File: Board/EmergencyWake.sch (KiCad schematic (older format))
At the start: 138 parts, among them J1 USB_C_Receptacle_USB2.0, J10 Conn_01x04, J2 Micro_SD_Card_Det, J3 Conn_01x03, J4 Conn_01x02, J5 Conn_01x05, J6 Conn_01x04, J7 Conn_01x02, J8 Conn_01x04, J9 Conn_01x04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

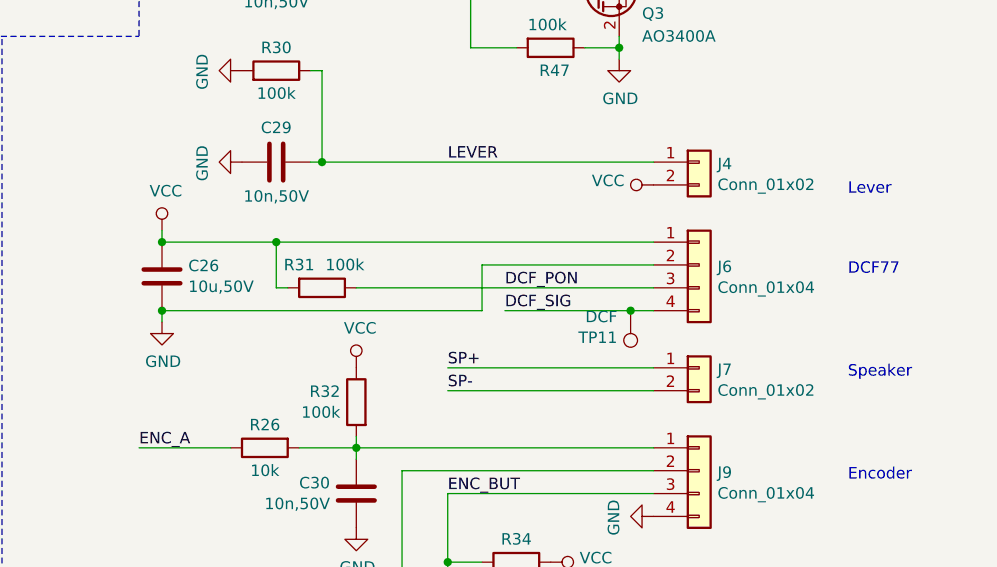
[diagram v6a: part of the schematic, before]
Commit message: [Board] More routing
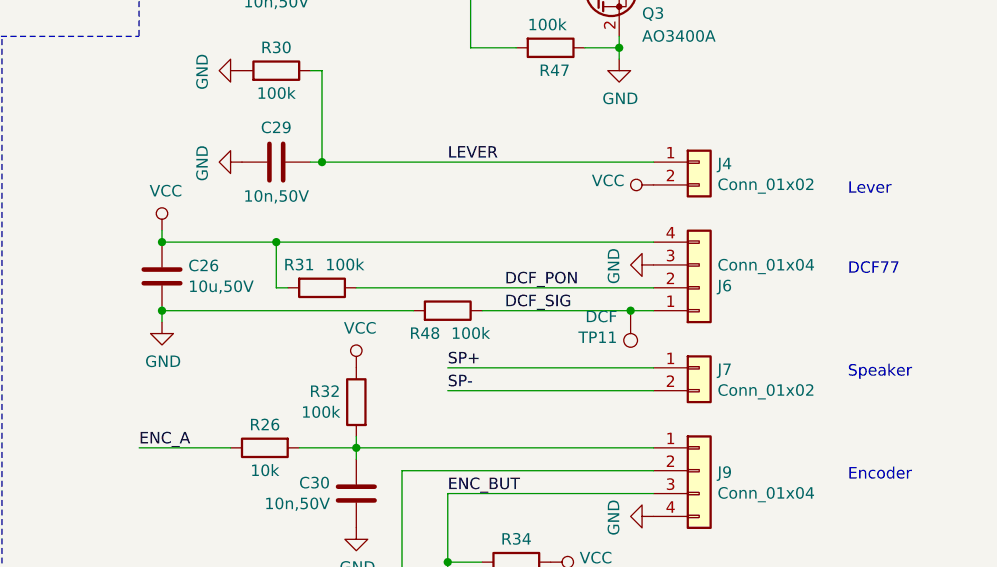
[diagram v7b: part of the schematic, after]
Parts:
- added R48: 100k, Resistor_SMD:R_0402_1005Metric, symbol Device:R
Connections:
- net DCF_PON: now also J6.2 (Pin_2); no longer J6.3 (Pin_3)
- net DCF_SIG: now also J6.1 (Pin_1), R48.1; no longer J6.4 (Pin_4)
- net GND: now also J6.3 (Pin_3), R48.2; no longer J6.2 (Pin_2)
- net VCC: now also J6.4 (Pin_4); no longer J6.1 (Pin_1)
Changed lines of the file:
@@
 L Connector_Generic:Conn_01x04 J6
 U 1 1 5E489DA8
-P 13900 3300
-F 0 "J6" H 13980 3292 50  0000 L CNN
-F 1 "Conn_01x04" H 13980 3201 50  0000 L CNN
-F 2 "Connector_PinHeader_2.54mm:PinHeader_1x04_P2.54mm_Horizontal" H 13900 3300 50  0001 C CNN
-F 3 "~" H 13900 3300 50  0001 C CNN
-	1    13900 3300
-	1    0    0    -1
+P 13900 3400
+F 0 "J6" H 13980 3392 50  0000 L CNN
+F 1 "Conn_01x04" H 13980 3301 50  0000 L CNN
+F 2 "Connector_PinHeader_2.54mm:PinHeader_1x04_P2.54mm_Horizontal" H 13900 3400 50  0001 C CNN
+F 3 "~" H 13900 3400 50  0001 C CNN
+	1    13900 3400
+	1    0    0    1
 $EndComp
-Wire Wire Line
-	13050 3500 13600 3500
 Text Label 13050 3400 0    50   ~ 0
 DCF_PON
@@
 Wire Wire Line
 	11550 3550 11550 3500
-Wire Wire Line
-	12950 3500 12950 3300
-Wire Wire Line
-	12950 3300 13700 3300
 $Comp
 L Device:R R31
@@
 Wire Wire Line
 	11450 5250 11850 5250
-Connection ~ 11550 3500
 Connection ~ 12050 3200
 $Comp
@@
 	12050 3200 13700 3200
 Wire Wire Line
-	11550 3500 12950 3500
-$Comp
-L VFD:FUTABA_4-LT-46ZB3 DISP1
-U 1 1 5E418818
-P 14000 6600
-F 0 "DISP1" H 14000 7115 50  0000 C CNN
-F 1 "FUTABA_4-LT-46ZB3" H 14000 7024 50  0000 C CNN
-F 2 "VFD:FUTABA_4-LT-46ZB3" H 14000 5150 50  0001 C CNN
-F 3 "https://www.pollin.de/productdownloads/D121537D.PDF" V 14050 7450 50  0001 C CNN
-	1    14000 6600
-	1    0    0    -1
-$EndComp
-Wire Wire Line
 	15150 7500 15350 7500
 Wire Wire Line
@@
 NoConn ~ 7150 4600
 NoConn ~ 7150 4700
+$Comp
+L power:GND #PWR0102
+U 1 1 5E4F1DFC
+P 13700 3300
+F 0 "#PWR0102" H 13700 3050 50  0001 C CNN
+F 1 "GND" H 13705 3127 50  0000 C CNN
+F 2 "" H 13700 3300 50  0001 C CNN
+F 3 "" H 13700 3300 50  0001 C CNN
+	1    13700 3300
+	0    1    1    0
+$EndComp
+$Comp
+L Device:R R48
+U 1 1 5E4F3188
+P 12800 3500
+F 0 "R48" V 12700 3400 50  0000 C CNN
+F 1 "100k" V 12700 3600 50  0000 C CNN
+F 2 "Resistor_SMD:R_0402_1005Metric" V 12730 3500 50  0001 C CNN
+F 3 "~" H 12800 3500 50  0001 C CNN
+F 4 "C25741" H 12800 3500 50  0001 C CNN "LCSC"
+	1    12800 3500
+	0    1    -1   0
+$EndComp
+Wire Wire Line
+	12950 3500 13600 3500
+Wire Wire Line
+	12650 3500 11550 3500
+Connection ~ 11550 3500
+$Comp
+L VFD:FUTABA_4-LT-46ZB3 DISP1
+U 1 1 5E418818
+P 14000 6600
+F 0 "DISP1" H 14000 7115 50  0000 C CNN
+F 1 "FUTABA_4-LT-46ZB3" H 14000 7024 50  0000 C CNN
+F 2 "VFD:FUTABA_4-LT-46ZB3" H 14000 5150 50  0001 C CNN
+F 3 "https://www.pollin.de/productdownloads/D121537D.PDF" V 14050 7450 50  0001 C CNN
+	1    14000 6600
+	1    0    0    -1
+$EndComp
 $EndSCHEMATC

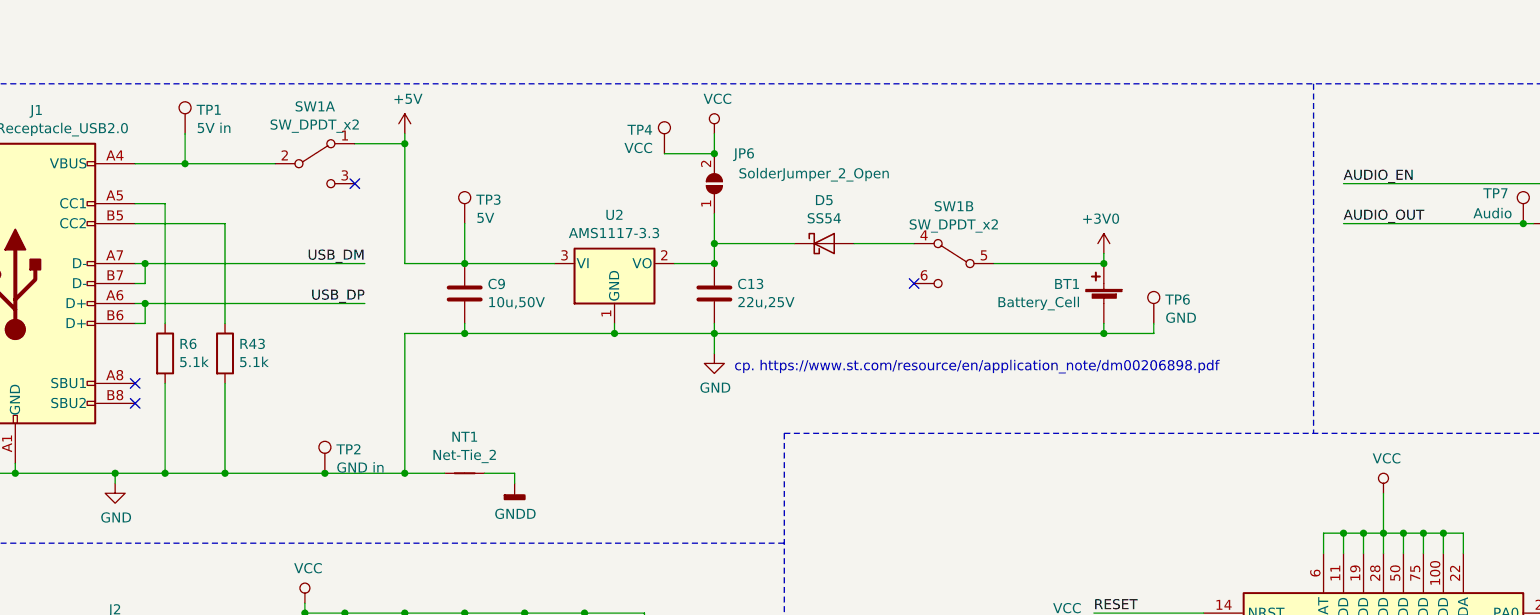
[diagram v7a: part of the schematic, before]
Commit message: [Board] Added TVS diodes for USB
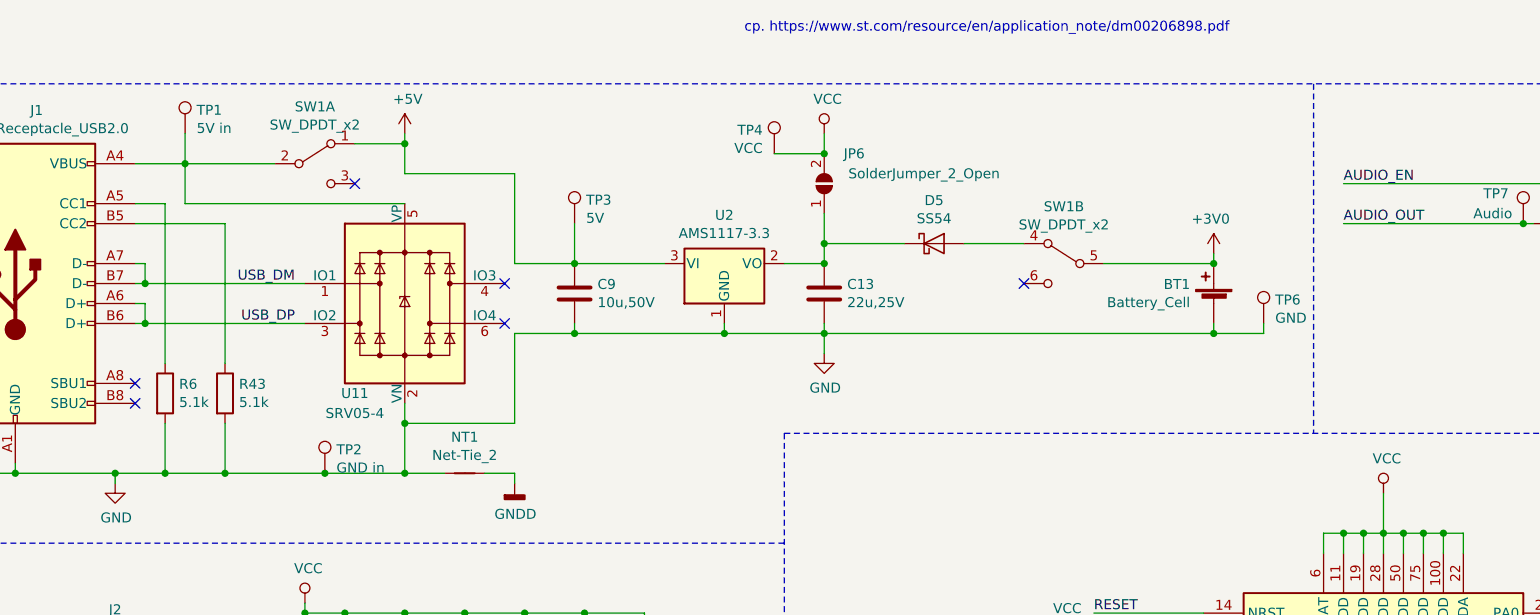
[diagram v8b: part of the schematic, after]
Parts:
- added U11: SRV05-4, Package_TO_SOT_SMD:SOT-23-6, symbol Power_Protection:SRV05-4
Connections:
- net GND: now also U11.2 (VN)
- net USB_DM: now also U11.1 (IO1)
- net USB_DP: now also U11.3 (IO2)
- net at J1.A4 (VBUS), J1.A9 (VBUS), J1.B4 (VBUS)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: now also U11.5 (VP)
- no-connect marks 54 -> 56
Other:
- moved on the sheet: BT1, C13, C9, D5, JP6, R43, R6, SW1B, TP3, TP4, TP6, U2
